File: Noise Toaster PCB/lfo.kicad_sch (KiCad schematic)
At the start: 12 parts, among them J4 LFO, U2 LM324

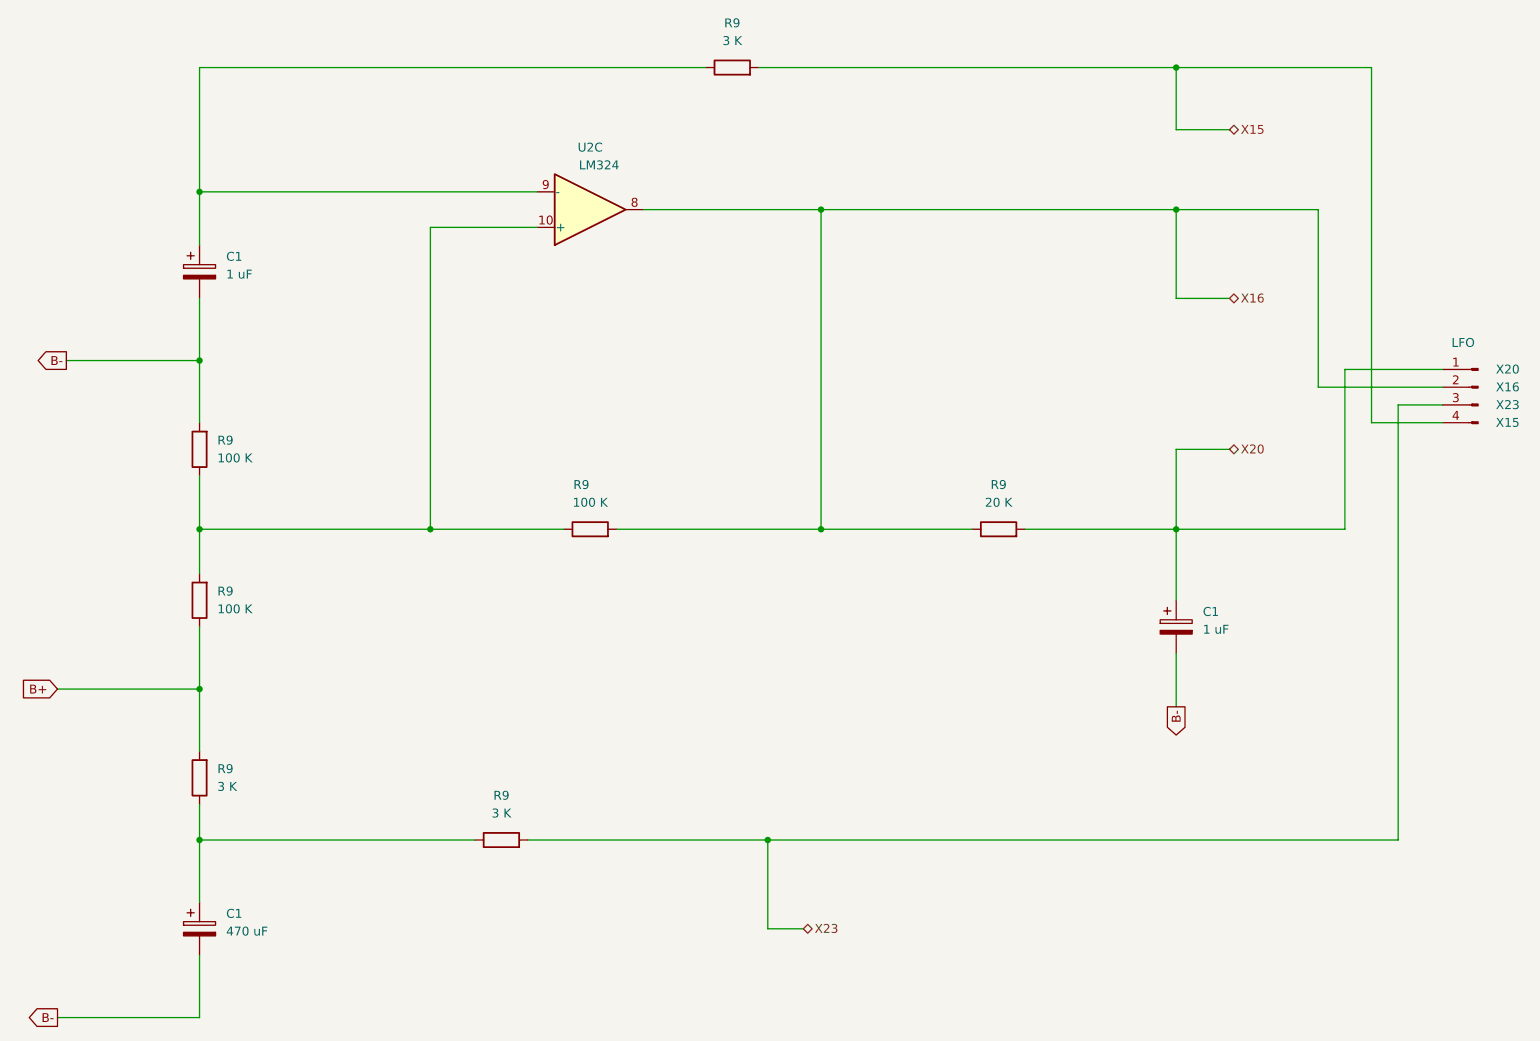
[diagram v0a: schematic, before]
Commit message: added front panel pcb
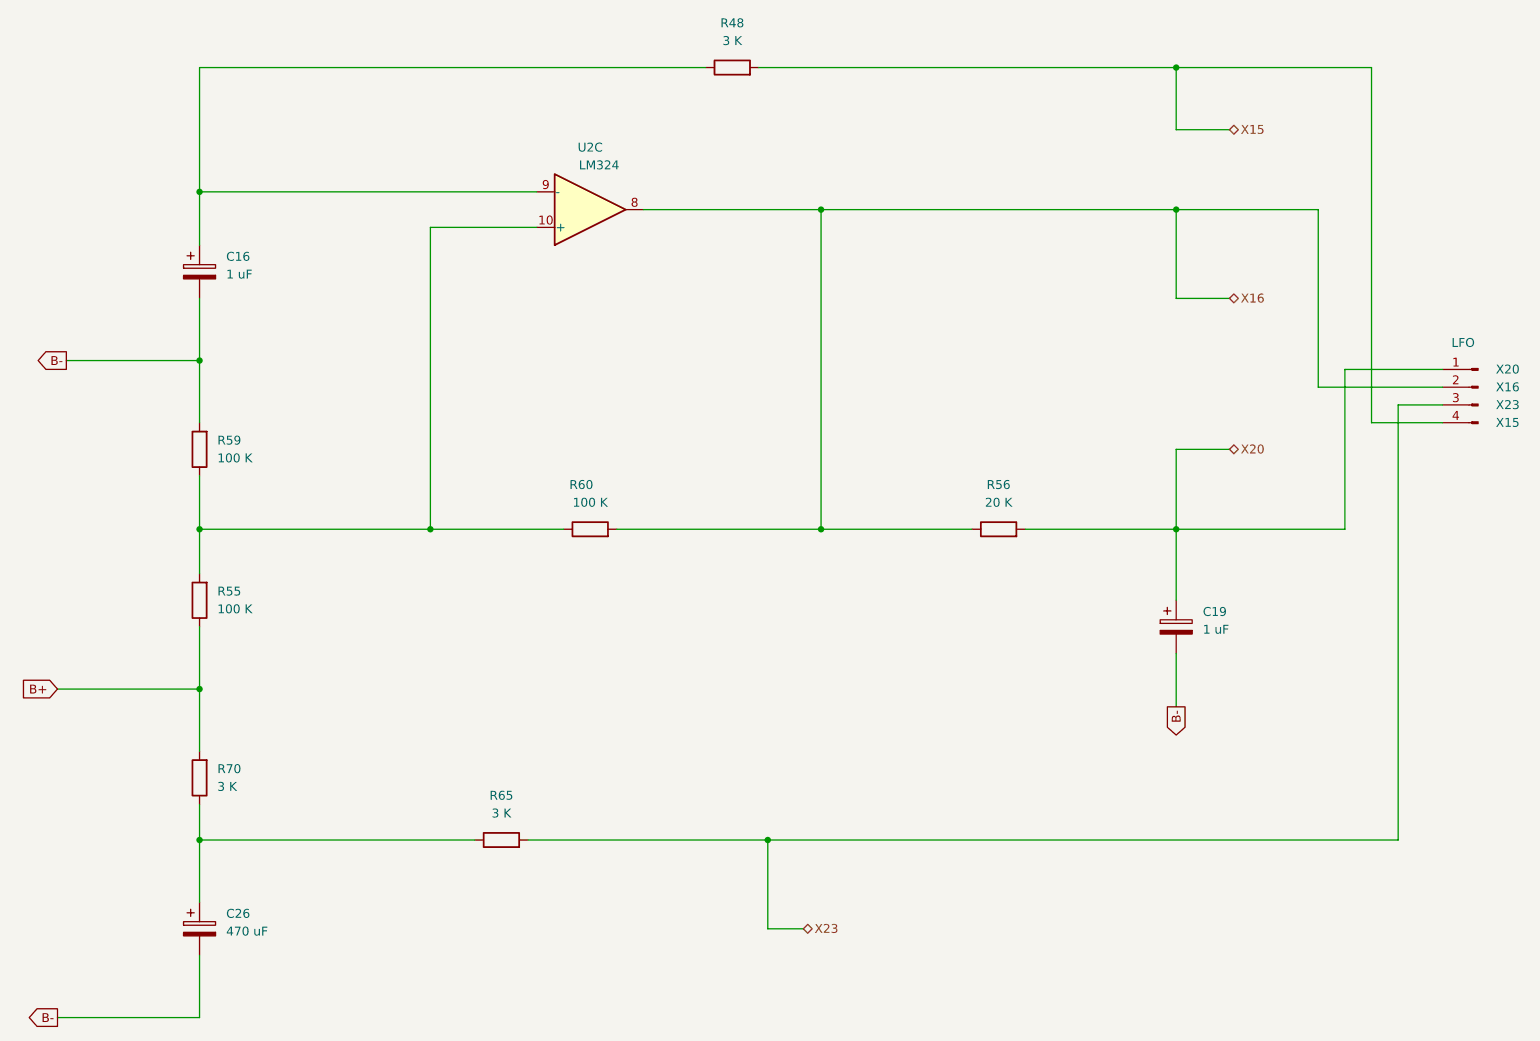
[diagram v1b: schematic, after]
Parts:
- renumbered C1 to C16, C1 to C19, C1 to C26, R9 to R48, R9 to R55, R9 to R56, R9 to R59, R9 to R60, R9 to R65, R9 to R70
